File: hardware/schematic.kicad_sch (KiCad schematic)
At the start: 9 parts, among them J3 Connector_1, U1 ESP32-S3-DevKitC, U2 TJA1050_module

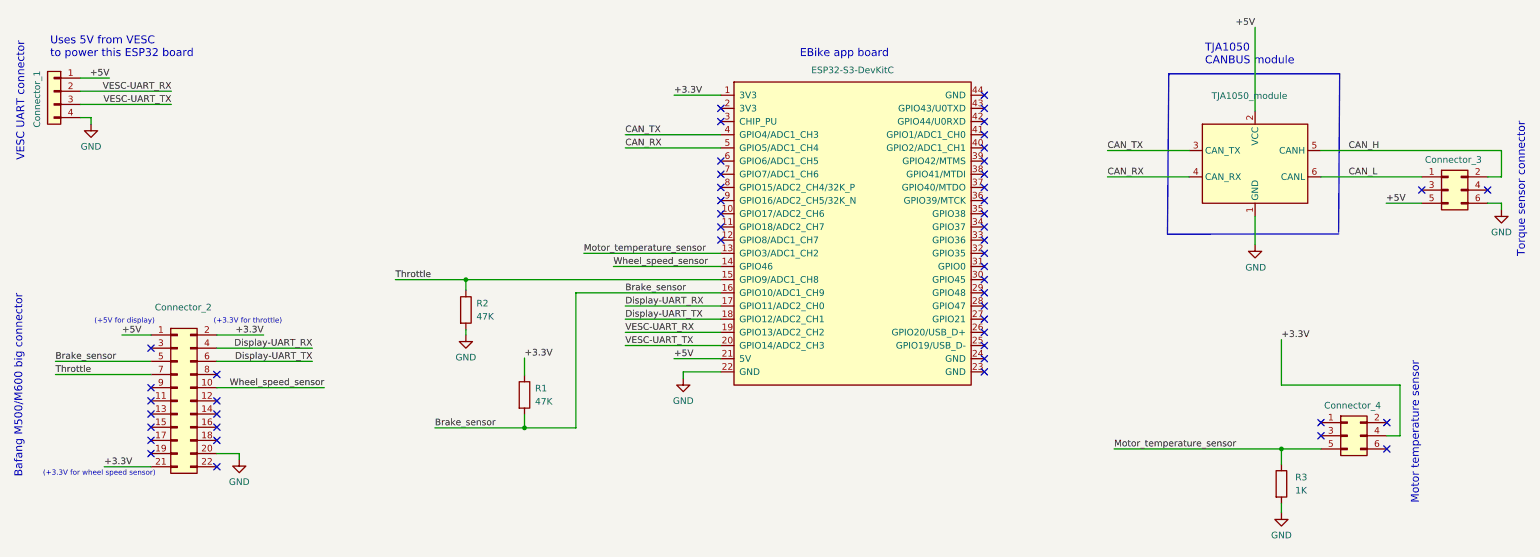
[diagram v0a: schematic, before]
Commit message: Added latest schematic version as also the testing_sensors code, including a screenshot of the sensors output
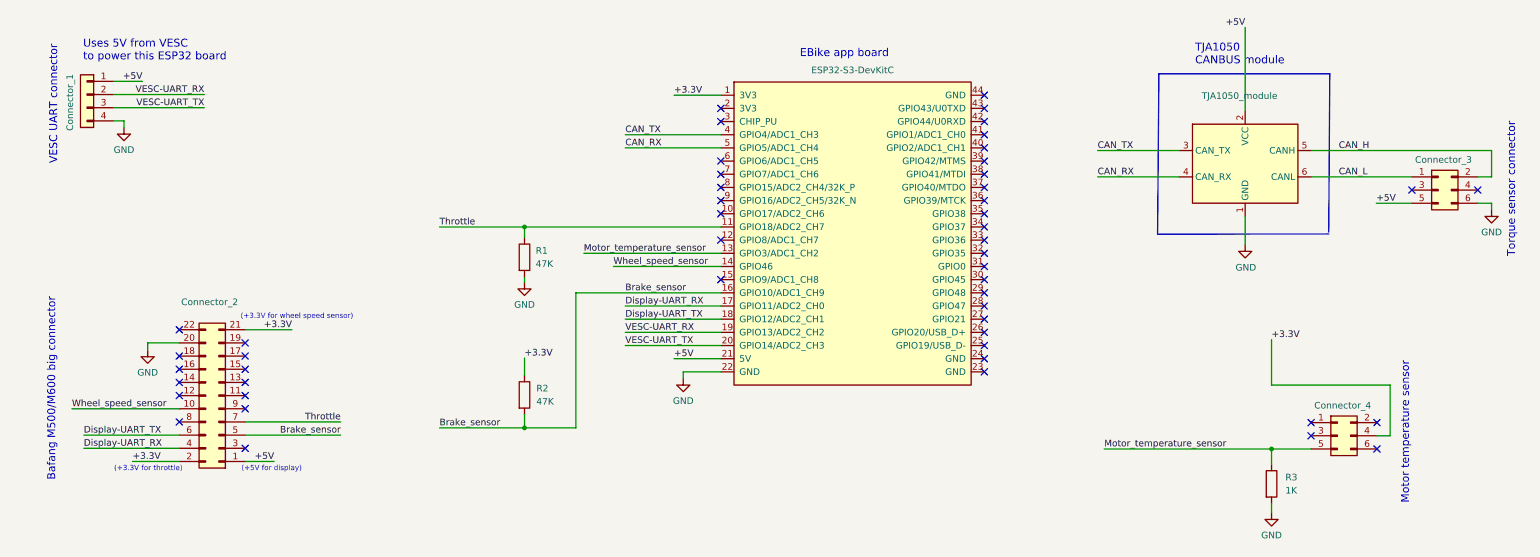
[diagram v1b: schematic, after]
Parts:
- removed R2: 47K, symbol Device:R
- added R1: 47K, symbol Device:R
- renumbered R1 to R2
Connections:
- net GND: now also R1.2
- net Throttle: now also U1.11 (GPIO18/ADC2_CH7), R1.1; no longer U1.15 (GPIO9/ADC1_CH8)
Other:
- moved on the sheet: Connector_2, Connector_3, Connector_4, R3
